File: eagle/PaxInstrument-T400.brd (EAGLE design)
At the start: 96.5 x 50.8 mm, 128 parts, among them IC1 MCP3424, U1 MCP9800, U2 HTU21DSMD, U3 MCP73831, U4 MIC5219-3.3V, U6 MPL3115A2LGA8, U7 USD-SOCKETNEW, U8 NC7S32, X2 FH12-12S-0.5SH, Y1 RESONATORSMD

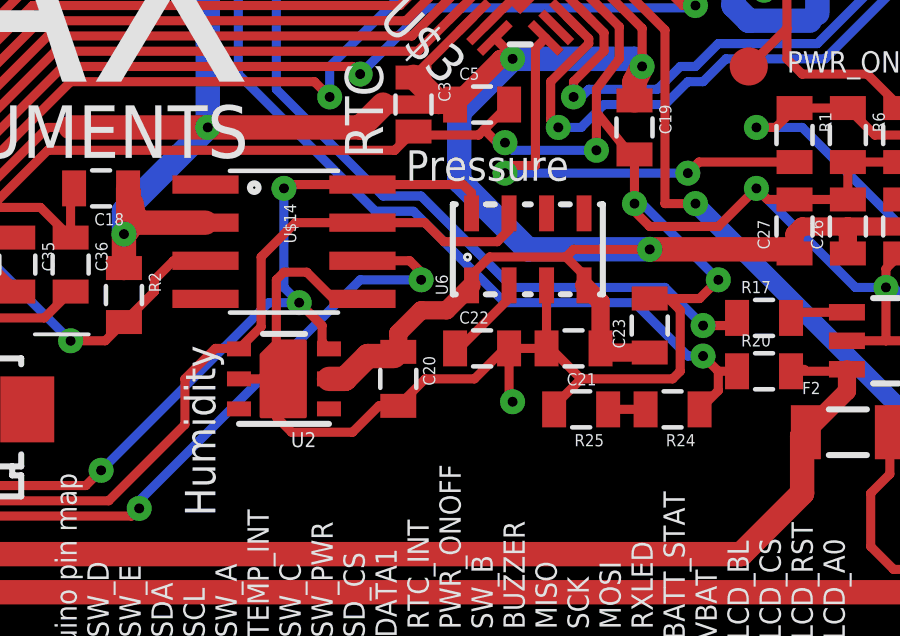
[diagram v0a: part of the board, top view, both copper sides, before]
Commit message: - Removed pressure and humidity sensors - updated .gitignore
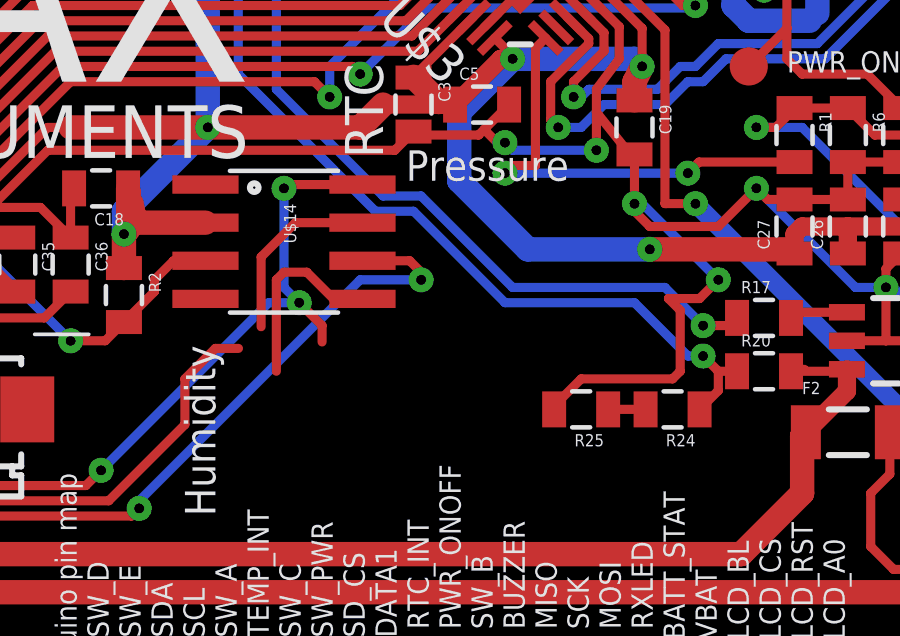
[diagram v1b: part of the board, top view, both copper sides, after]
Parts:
- removed C20, C21, C22: 0.1uF, SparkFun-Passives:0805
- removed C23: 1uF, SparkFun-Passives:0805
- removed U2: HTU21DSMD, SparkFun-Sensors:HTU21D
- removed U6: MPL3115A2LGA8, SparkFun-Sensors:LGA8
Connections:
- removed net N$8: C22.1, U6.2
- net 3.3V: no longer C20.1, C21.1, C23.1, U2.VDD, U6.1, U6.4
- net GND: no longer C20.2, C21.2, C22.2, C23.2, U2.7, U2.GND, U6.3
- net SCL: no longer U2.SCK, U6.8
- net SDA: no longer U2.DATA, U6.7
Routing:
- net GND: track 527.0 -> 506.9 mm, vias 43 -> 42
- net 3.3V: track 383.6 -> 365.6 mm
- net SDA: track 166.1 -> 159.2 mm
- net SCL: track 175.7 -> 170.9 mm
- net N$8: track 2.93 -> 0.00 mm

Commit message: - Removed buzzer - Removed some traces - Nudged and schematic symbols
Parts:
- removed SG1: BUZZERSMD2, SparkFun-Electromechanical:BUZZER-CCV
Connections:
- net 3.3V: no longer SG1.+
- net BUZZER: no longer SG1.-
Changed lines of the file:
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@@
 <attribute name="OC_DIGIKEY" value="1276-5086-2-ND" x="82.55" y="31.496" size="1.778" layer="27" font="vector" ratio="15" display="off"/>
-</element>
-<element name="SG1" library="SparkFun-Electromechanical" package="BUZZER-CCV" value="BUZZERSMD2" x="19.05" y="29.21" rot="R180">
-<attribute name="MPN" value="CCV-084B16" x="19.05" y="29.21" size="1.778" layer="27" rot="R180" display="off"/>
-<attribute name="OC_DIGIKEY" value="102-1265-1-ND" x="19.05" y="29.21" size="1.778" layer="27" rot="R180" display="off"/>
 </element>
 <element name="U8" library="SparkFun-DigitalIC" package="SOT23-5" value="NC7S32" x="85.09" y="19.304" rot="R270">
@@
 <contactref element="ICSP1" pad="1"/>
 <wire x1="26.162" y1="19.05" x2="33.274" y2="19.05" width="0.8128" layer="1"/>
-<contactref element="SG1" pad="+"/>
 <contactref element="R29" pad="2"/>
 <contactref element="R27" pad="2"/>
@@
 <wire x1="77.724" y1="46.99" x2="79.502" y2="45.212" width="0.8128" layer="1"/>
 <wire x1="79.502" y1="45.212" x2="79.502" y2="44.08" width="0.8128" layer="1"/>
-<wire x1="15.05" y1="29.21" x2="14.796" y2="29.464" width="0.8128" layer="1"/>
 <wire x1="14.796" y1="29.464" x2="9.652" y2="29.464" width="0.8128" layer="1"/>
 <wire x1="8.89" y1="29.21" x2="9.144" y2="29.464" width="0.8128" layer="1"/>
@@
 </signal>
 <signal name="BUZZER">
-<contactref element="SG1" pad="-"/>
 <contactref element="U$3" pad="32"/>
 <wire x1="65.311490625" y1="28.12608125" x2="64.735571875" y2="28.702" width="0.3048" layer="1"/>
@@
 <wire x1="45.974" y1="19.304" x2="36.068" y2="19.304" width="0.3048" layer="16"/>
 <wire x1="36.068" y1="19.304" x2="35.814" y2="19.304" width="0.3048" layer="16"/>
-<wire x1="23.05" y1="29.21" x2="22.796" y2="28.956" width="0.3048" layer="1"/>
 <wire x1="22.796" y1="28.956" x2="20.574" y2="28.956" width="0.3048" layer="1"/>
 <via x="20.574" y="28.956" extent="1-16" drill="0.3302"/>

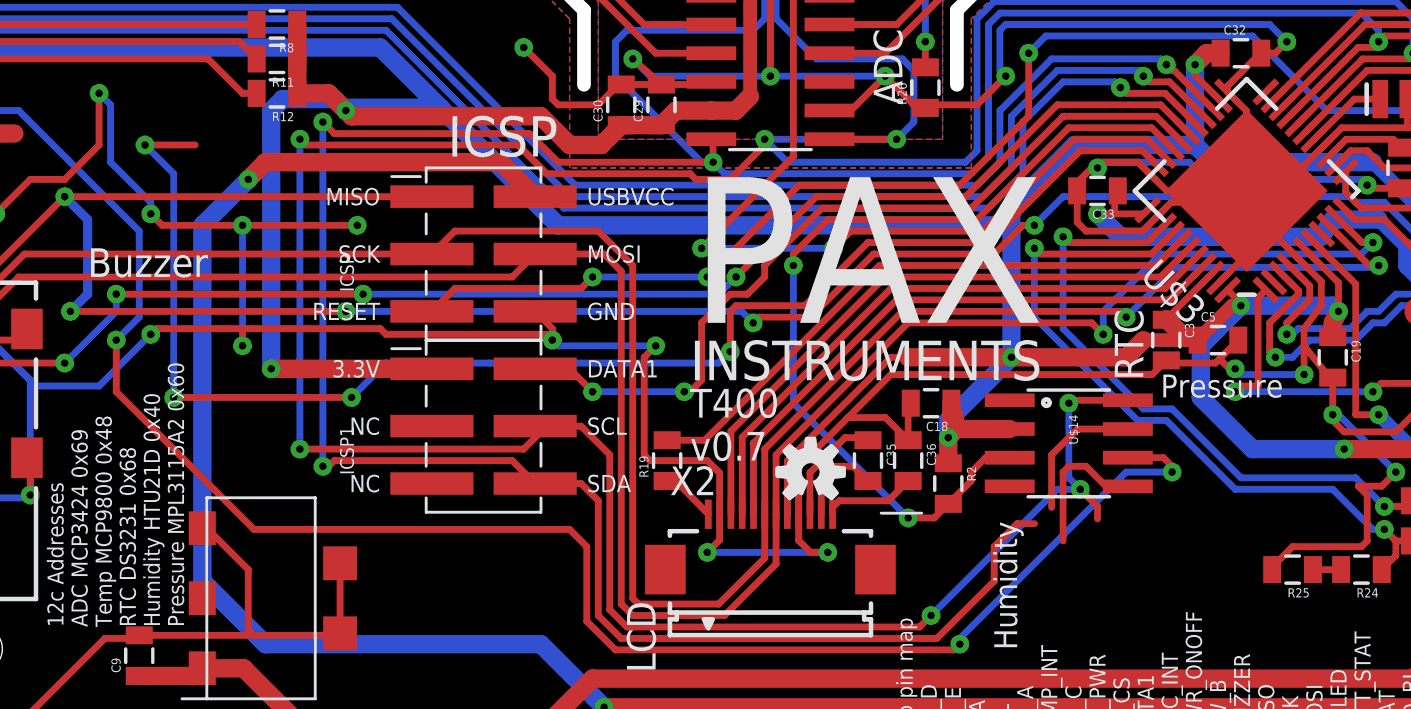
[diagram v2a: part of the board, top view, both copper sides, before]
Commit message: - Change the MCP73831 programming resistor 2k, so it will charge at 500 mA. - Buzzer pin reassigned to VBAT_EN. Bring VBAT_EN to measure VBAT. - LCD_BL now drains rather than sources LCD backlight power. - Battery outline removed
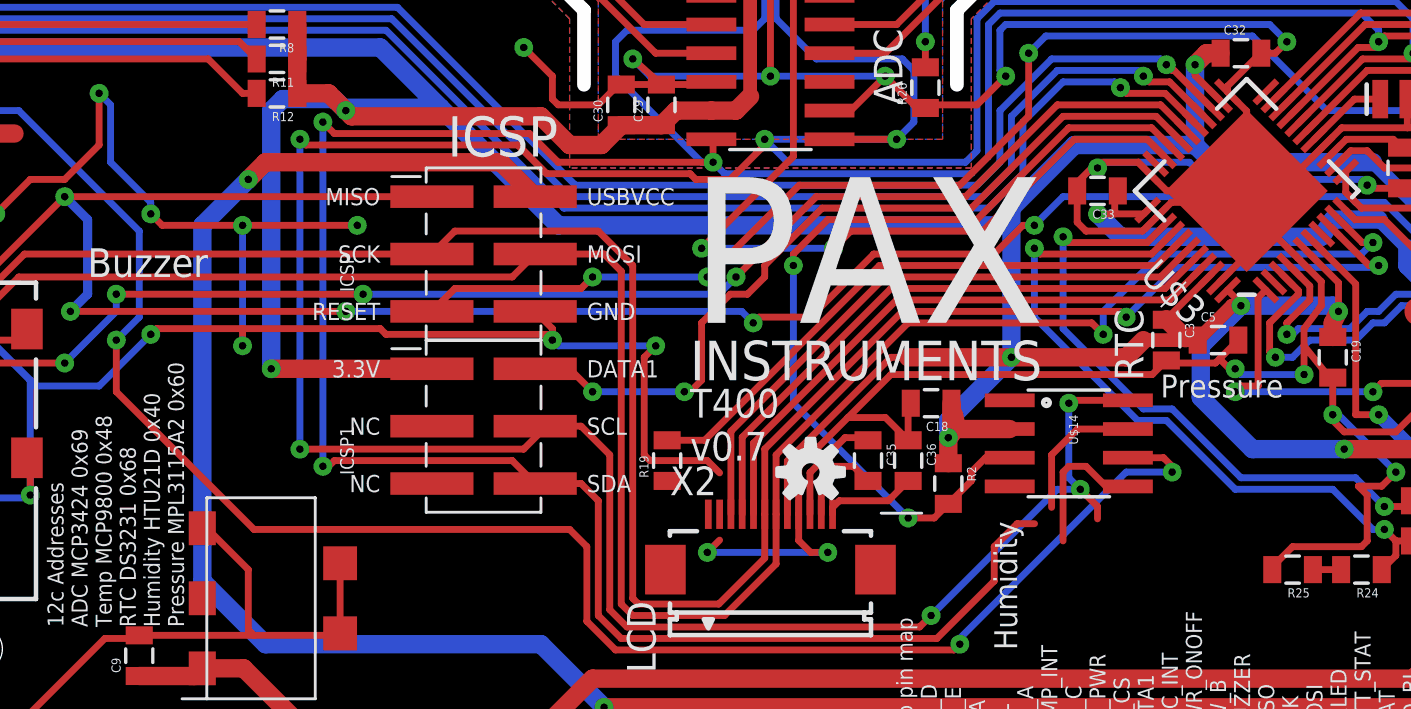
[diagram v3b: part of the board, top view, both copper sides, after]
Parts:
- R3: value 10k -> 2k
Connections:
- removed net BUZZER: U$3.32
- removed net N$29: R19.1, X2.1
- new net N$4: R19.1, X2.2
- new net VBAT_EN: R25.2, U$3.32
- net 3.3V: now also X2.1
- net GND: no longer R25.2, X2.2
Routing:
- net BUZZER: track 63.2 -> 0.00 mm, vias 4 -> 0
- net GND: track 506.9 -> 503.8 mm
- net N$29: track 2.44 -> 0.00 mm
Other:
- board text removed: "Battery"
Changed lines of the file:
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@@
 <layer number="28" name="bValues" color="7" fill="1" visible="no" active="yes"/>
 <layer number="29" name="tStop" color="7" fill="3" visible="yes" active="yes"/>
-<layer number="30" name="bStop" color="7" fill="6" visible="no" active="yes"/>
+<layer number="30" name="bStop" color="7" fill="6" visible="yes" active="yes"/>
 <layer number="31" name="tCream" color="7" fill="4" visible="yes" active="yes"/>
-<layer number="32" name="bCream" color="7" fill="5" visible="no" active="yes"/>
+<layer number="32" name="bCream" color="7" fill="5" visible="yes" active="yes"/>
 <layer number="33" name="tFinish" color="6" fill="3" visible="no" active="yes"/>
 <layer number="34" name="bFinish" color="6" fill="6" visible="no" active="yes"/>
@@
 <layer number="37" name="tTest" color="7" fill="1" visible="no" active="yes"/>
 <layer number="38" name="bTest" color="7" fill="1" visible="no" active="yes"/>
-<layer number="39" name="tKeepout" color="4" fill="11" visible="yes" active="yes"/>
+<layer number="39" name="tKeepout" color="4" fill="11" visible="no" active="yes"/>
 <layer number="40" name="bKeepout" color="1" fill="11" visible="no" active="yes"/>
 <layer number="41" name="tRestrict" color="4" fill="10" visible="no" active="yes"/>
@@
 <layer number="49" name="Reference" color="7" fill="1" visible="no" active="yes"/>
 <layer number="50" name="dxf" color="7" fill="1" visible="no" active="no"/>
-<layer number="51" name="tDocu" color="6" fill="1" visible="no" active="yes"/>
-<layer number="52" name="bDocu" color="7" fill="1" visible="no" active="yes"/>
+<layer number="51" name="tDocu" color="6" fill="1" visible="yes" active="yes"/>
+<layer number="52" name="bDocu" color="7" fill="1" visible="yes" active="yes"/>
 <layer number="53" name="tGND_GNDA" color="7" fill="9" visible="no" active="no"/>
 <layer number="54" name="bGND_GNDA" color="1" fill="9" visible="no" active="no"/>
@@
 <text x="40.132" y="13.97" size="0.762" layer="21" font="vector" ratio="15" align="center-left">SDA</text>
 <text x="40.132" y="16.51" size="0.762" layer="21" font="vector" ratio="15" align="center-left">SCL</text>
-<text x="81.28" y="6.35" size="1.778" layer="22" font="vector" ratio="15" rot="MR0">Battery</text>
 <text x="64.77" y="18.542" size="1.27" layer="21" font="vector" ratio="15" rot="R90">RTC</text>
 <text x="59.182" y="6.604" size="1.016" layer="21" font="vector" ratio="15" rot="R90">Humidity</text>
@@
 <text x="18.034" y="23.114" size="1.27" layer="21" font="vector" ratio="15">Buzzer</text>
 <text x="54.102" y="30.734" size="1.27" layer="21" font="vector" ratio="15" rot="R90">ADC</text>
-<wire x1="34.29" y1="35.56" x2="38.1" y2="35.56" width="0.3048" layer="22"/>
-<wire x1="82.55" y1="35.56" x2="78.74" y2="35.56" width="0.3048" layer="22"/>
-<wire x1="82.55" y1="35.56" x2="82.55" y2="31.75" width="0.3048" layer="22"/>
-<wire x1="82.55" y1="5.08" x2="82.55" y2="8.89" width="0.3048" layer="22"/>
-<wire x1="82.55" y1="5.08" x2="78.74" y2="5.08" width="0.3048" layer="22"/>
-<wire x1="34.29" y1="5.08" x2="38.1" y2="5.08" width="0.3048" layer="22"/>
-<wire x1="34.29" y1="35.56" x2="34.29" y2="31.75" width="0.3048" layer="22"/>
-<wire x1="34.29" y1="5.08" x2="34.29" y2="8.89" width="0.3048" layer="22"/>
 <text x="53.848" y="0.762" size="0.7112" layer="21" font="vector" ratio="15" rot="R90" align="top-left">Arduino pin map
 D0  SW_D
@@
 <attribute name="OC_DIGIKEY" value="490-3297-2-ND" x="20.32" y="6.35" size="1.778" layer="27" rot="R90" display="off"/>
 </element>
-<element name="R3" library="SparkFun-Passives" package="0805" value="10k" x="84.582" y="12.446" rot="R270">
+<element name="R3" library="SparkFun-Passives" package="0805" value="2k" x="84.582" y="12.446" rot="R270">
 <attribute name="OC_DIGIKEY" value="1276-5086-2-ND" x="84.582" y="12.446" size="1.778" layer="27" rot="R270" display="off"/>
 </element>
@@
 <wire x1="27.316" y1="31.242" x2="28.702" y2="31.242" width="0.8128" layer="1"/>
 <wire x1="28.702" y1="31.242" x2="29.464" y2="30.48" width="0.8128" layer="1"/>
+<contactref element="X2" pad="1"/>
+<wire x1="49.01" y1="12.61" x2="45.51" y2="12.61" width="0" layer="19" extent="1-1"/>
 </signal>
 <signal name="3V3EN">
@@
 <contactref element="S4" pad="1"/>
 <contactref element="S5" pad="1"/>
-<contactref element="X2" pad="2"/>
 <contactref element="X2" pad="9"/>
 <contactref element="C36" pad="1"/>
@@
 <wire x1="67.956" y1="19.304" x2="65.902" y2="19.304" width="0.3048" layer="1"/>
 <wire x1="65.902" y1="19.304" x2="65.786" y2="19.42" width="0.3048" layer="1"/>
-<wire x1="46.01" y1="12.61" x2="46.01" y2="14.442" width="0.3048" layer="1"/>
 <wire x1="46.01" y1="14.442" x2="45.466" y2="14.986" width="0.3048" layer="1"/>
 <wire x1="49.51" y1="12.61" x2="49.51" y2="14.712" width="0.3048" layer="1"/>
@@
 <wire x1="86.614" y1="6.858" x2="87.376" y2="7.62" width="0.3048" layer="1"/>
 <wire x1="87.376" y1="7.62" x2="90.816" y2="7.62" width="0.3048" layer="1"/>
-<wire x1="46.01" y1="12.61" x2="46.01" y2="11.466" width="0.3048" layer="1"/>
 <wire x1="46.01" y1="11.466" x2="45.466" y2="10.922" width="0.3048" layer="1"/>
 <via x="45.466" y="10.922" extent="1-16" drill="0.3302"/>
@@
 <wire x1="50.038" y1="10.922" x2="50.8" y2="10.922" width="0.3048" layer="1"/>
 <wire x1="90.816" y1="7.62" x2="91.694" y2="8.498" width="0.3048" layer="1"/>
-<wire x1="70.358" y1="12.192" x2="71.374" y2="11.176" width="0" layer="19" extent="1-16"/>
 <wire x1="71.374" y1="11.176" x2="74.422" y2="11.176" width="0.3048" layer="1"/>
 <contactref element="U$1" pad="PIN$5"/>
@@
 <wire x1="55.118" y1="30.596" x2="54.748" y2="30.596" width="0.3048" layer="1"/>
 <wire x1="54.748" y1="30.596" x2="54.61" y2="30.734" width="0.3048" layer="1"/>
-<contactref element="R25" pad="2"/>
 <contactref element="U$2" pad="P$3"/>
 <contactref element="U$2" pad="P$4"/>
 <contactref element="U$2" pad="P$5"/>
-<wire x1="70.474" y1="10.16" x2="70.474" y2="10.276" width="0.3048" layer="1"/>
 <wire x1="70.474" y1="10.276" x2="71.374" y2="11.176" width="0.3048" layer="1"/>
 <wire x1="15.494" y1="13.462" x2="15.494" y2="13.256" width="0.3048" layer="1"/>
@@
 <wire x1="18.542" y1="28.956" x2="18.542" y2="31.242" width="0.3048" layer="1"/>
 <wire x1="65.162" y1="18.796" x2="62.23" y2="14.732" width="0" layer="19" extent="1-1"/>
+<wire x1="46.01" y1="14.442" x2="46.01" y2="11.466" width="0" layer="19" extent="1-1"/>
 </signal>
 <signal name="USBVCC">
@@
 <wire x1="9.398" y1="37.846" x2="6.985" y2="37.846" width="0.3048" layer="16"/>
 <wire x1="25.516" y1="34.29" x2="9.398" y2="34.29" width="0.3048" layer="1"/>
-</signal>
-<signal name="BUZZER">
-<contactref element="U$3" pad="32"/>
-<wire x1="65.311490625" y1="28.12608125" x2="64.735571875" y2="28.702" width="0.3048" layer="1"/>
-<wire x1="64.735571875" y1="28.702" x2="61.976" y2="28.702" width="0.3048" layer="1"/>
-<wire x1="61.976" y1="28.702" x2="57.912" y2="24.638" width="0.3048" layer="1"/>
-<wire x1="57.912" y1="24.638" x2="52.578" y2="24.638" width="0.3048" layer="1"/>
-<wire x1="52.578" y1="24.638" x2="49.784" y2="21.844" width="0.3048" layer="1"/>
-<wire x1="49.784" y1="21.844" x2="46.736" y2="21.844" width="0.3048" layer="1"/>
-<wire x1="46.736" y1="21.844" x2="46.482" y2="21.59" width="0.3048" layer="1"/>
-<wire x1="46.482" y1="21.59" x2="46.482" y2="19.812" width="0.3048" layer="1"/>
-<via x="46.482" y="19.812" extent="1-16" drill="0.3302"/>
-<wire x1="46.482" y1="19.812" x2="45.974" y2="19.304" width="0.3048" layer="16"/>
-<wire x1="45.974" y1="19.304" x2="36.068" y2="19.304" width="0.3048" layer="16"/>
-<wire x1="36.068" y1="19.304" x2="35.814" y2="19.304" width="0.3048" layer="16"/>
-<wire x1="22.796" y1="28.956" x2="20.574" y2="28.956" width="0.3048" layer="1"/>
-<via x="20.574" y="28.956" extent="1-16" drill="0.3302"/>
-<wire x1="20.574" y1="28.956" x2="21.844" y2="27.686" width="0.3048" layer="16"/>
-<wire x1="21.844" y1="27.686" x2="21.844" y2="17.78" width="0.3048" layer="16"/>
-<via x="21.844" y="17.78" extent="1-16" drill="0.3302"/>
-<wire x1="21.844" y1="17.78" x2="29.718" y2="17.78" width="0.3048" layer="1"/>
-<via x="29.718" y="17.78" extent="1-16" drill="0.3302"/>
-<wire x1="29.718" y1="17.78" x2="31.242" y2="19.304" width="0.3048" layer="16"/>
-<wire x1="31.242" y1="19.304" x2="35.814" y2="19.304" width="0.3048" layer="16"/>
 </signal>
 <signal name="ISOTHERMAL">
@@
 <wire x1="78.74" y1="19.558" x2="84.074" y2="14.224" width="0.3048" layer="16"/>
 </signal>
-<signal name="N$29">
-<contactref element="X2" pad="1"/>
-<contactref element="R19" pad="1"/>
-<wire x1="45.51" y1="12.61" x2="44.072" y2="14.086" width="0.3048" layer="1"/>
-<wire x1="44.072" y1="14.086" x2="43.688" y2="14.086" width="0.3048" layer="1"/>
-</signal>
 <signal name="N$37">
 <contactref element="X2" pad="10"/>
@@
 <wire x1="84.21" y1="4.826" x2="85.226" y2="5.842" width="0.3048" layer="1"/>
 </signal>
+<signal name="VBAT_EN">
+<contactref element="R25" pad="2"/>
+<contactref element="U$3" pad="32"/>
+<wire x1="70.474" y1="10.16" x2="65.311490625" y2="28.12608125" width="0" layer="19" extent="1-1"/>
+</signal>
+<signal name="N$4">
+<contactref element="X2" pad="2"/>
+<contactref element="R19" pad="1"/>
+<wire x1="43.688" y1="14.086" x2="46.01" y2="12.61" width="0" layer="19" extent="1-1"/>
+</signal>
 </signals>
